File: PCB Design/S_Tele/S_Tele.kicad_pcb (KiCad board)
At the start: 2 copper layers, 126.7 x 46 mm, 38 parts, among them J1 Screw_Terminal_01x08, J2 Conn_01x01, J3 SMA, J4 SMA, J5 SMA, J6 SMA, J7 SMA, J8 SMA, U1 L7815, U2 L7805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

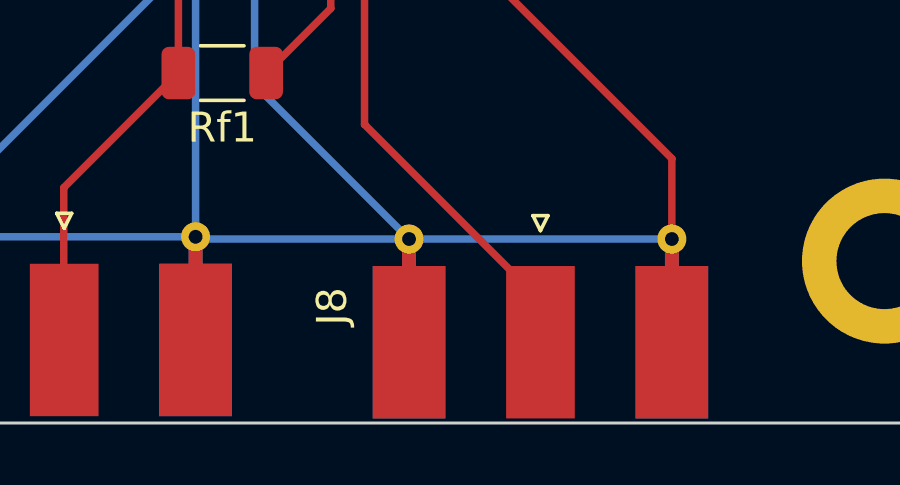
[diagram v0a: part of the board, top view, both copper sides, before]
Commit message: Added output scaling circuit to report
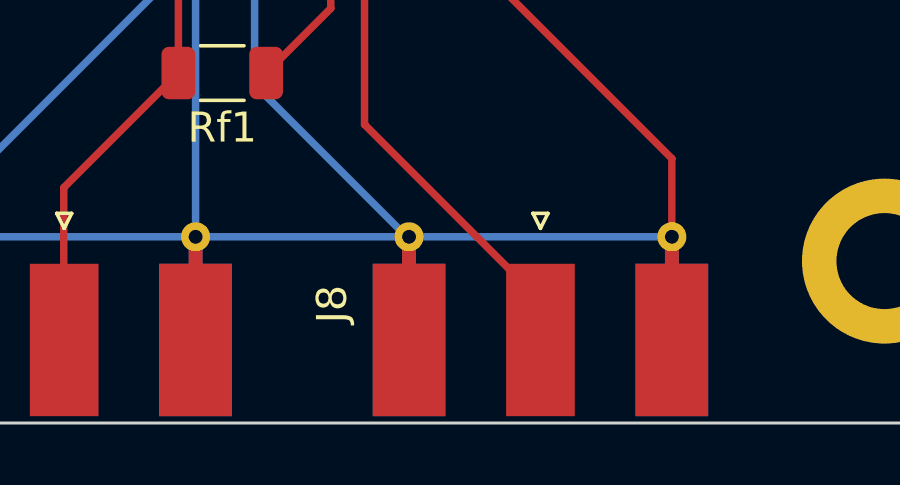
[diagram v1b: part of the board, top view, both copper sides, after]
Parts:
- moved J8 0.08 mm to (180.0, 115.2)
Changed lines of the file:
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@@
   )
   (footprint "Connector_Coaxial:SMA_Molex_73251-1153_EdgeMount_Horizontal" (layer "F.Cu")
-    (at 180.0484 115.2844 90)
+    (at 180.0484 115.2094 90)
     (descr "Molex SMA RF Connectors, Edge Mount, (http://www.molex.com/pdm_docs/sd/732511150_sd.pdf)")
     (tags "sma edge")
@@
   (segment (start 184.4356 113.5716) (end 184.4284 113.5644) (width 0.25) (layer "B.Cu") (net 2))
   (segment (start 170.5192 102.8864) (end 170.5192 102.05335) (width 0.25) (layer "B.Cu") (net 2))
-  (segment (start 175.6684 113.5644) (end 168.6284 113.5644) (width 0.25) (layer "B.Cu") (net 2))
   (segment (start 103.6325 110.64875) (end 105.283 110.64875) (width 0.8) (layer "B.Cu") (net 2))
   (segment (start 168.5532 80.05585) (end 175.6682 80.05585) (width 0.25) (layer "B.Cu") (net 2))
@@
   (segment (start 184.4282 80.05585) (end 175.6682 80.05585) (width 0.25) (layer "B.Cu") (net 2))
   (segment (start 170.5192 102.05335) (end 159.7934 112.77915) (width 0.25) (layer "B.Cu") (net 2))
-  (segment (start 184.4284 113.5644) (end 175.6684 113.5644) (width 0.25) (layer "B.Cu") (net 2))
+  (segment (start 168.5534 113.4894) (end 184.4284 113.4894) (width 0.25) (layer "B.Cu") (net 2))
   (segment (start 119.677067 102.52075) (end 122.428 102.52075) (width 0.8) (layer "F.Cu") (net 3))
   (segment (start 108.458 108.53775) (end 108.633 108.36275) (width 0.8) (layer "F.Cu") (net 3))
